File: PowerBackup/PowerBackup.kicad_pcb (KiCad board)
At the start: 4 copper layers, 40 x 41 mm, 70 parts, among them J1 Conn_01x02_Female, J10 Conn_01x02_Female, J2 Conn_01x07_Male, J3 Conn_01x04_Male, J4 Conn_01x05_Female, J5 Conn_01x04_Male, J6 Conn_01x02_Female, J7 Conn_01x02_Male, J8 Conn_01x02_Female, J9 Conn_01x02_Female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

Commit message: Added BOM and production files
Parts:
- added R24: 100, Resistor_SMD:R_0805_2012Metric, B.Cu at (131.0, 105.6)
- R12, R9: footprint Resistor_SMD:R_0805_2012Metric -> Resistor_SMD:R_0603_1608Metric
- R14: value 200 -> 100
- R18: value 1.5k -> 1k
- TH1: value Thermistor_NTC -> 10k
- moved R14 2.85 mm to (128.2, 106.3), turned to -90 degrees
- moved C18 0.23 mm to (126.5, 98.8)
- moved R21 0.22 mm to (123.7, 100.1)
- moved J9 0.18 mm to (124.1, 115.3)
- moved C16 0.17 mm to (129.2, 98.4)
- moved C17 0.17 mm to (130.7, 98.4)
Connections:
- net Net-(J3-Pad3) renamed /PrimaryBatteryMonitoring/SDA
- net Net-(J3-Pad4) renamed /PrimaryBatteryMonitoring/SCL
- C1 pad 2: GNDS -> GND
- C11 pad 2: GNDS -> GND
- C2 pad 2: GNDS -> GND
- C25 pad 2: GNDS -> GND
- C3 pad 2: GNDS -> GND
- C4 pad 2: GNDS -> GND
- C5 pad 2: GNDS -> GND
- C6 pad 2: GNDS -> GND
- C7 pad 2: GNDS -> GND
- C8 pad 2: GNDS -> GND
- C9 pad 2: GNDS -> GND
- J3 pad 1: GNDS -> GND
- J5 pad 1: GNDS -> GND
- R10 pad 2: GNDS -> GND
- R12 pad 2: GNDS -> GND
- R23 pad 2: GNDS -> GND
- TH1 pad 2: GNDS -> GND
- U1 pad 10: GNDS -> GND
- U1 pad 16: Net-(R14-Pad1) -> Net-(R24-Pad1)
- U2 pad 23: GNDS -> GND
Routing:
- net GND: track 14.0 -> 17.8 mm, vias 29 -> 88
- net GNDS: track 3.78 -> 0.00 mm, vias 32 -> 0
- net Net-(R24-Pad1): track 0.00 -> 2.90 mm
- net Net-(J4-Pad2): track 7.33 -> 8.47 mm
- net Net-(R14-Pad1): track 2.90 -> 2.19 mm
- added copper zone on In2.Cu, net GND
- removed copper zone on B.Cu, net GNDS
- removed copper zone on F.Cu, net GNDS
- removed copper zone on In2.Cu, net GNDS
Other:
- board text added: "+5V"
- board text added: "+9V"
- board text added: "GND"
- board text added: "SCL"
- board text added: "SDA"
- board text added: "VBAT+"

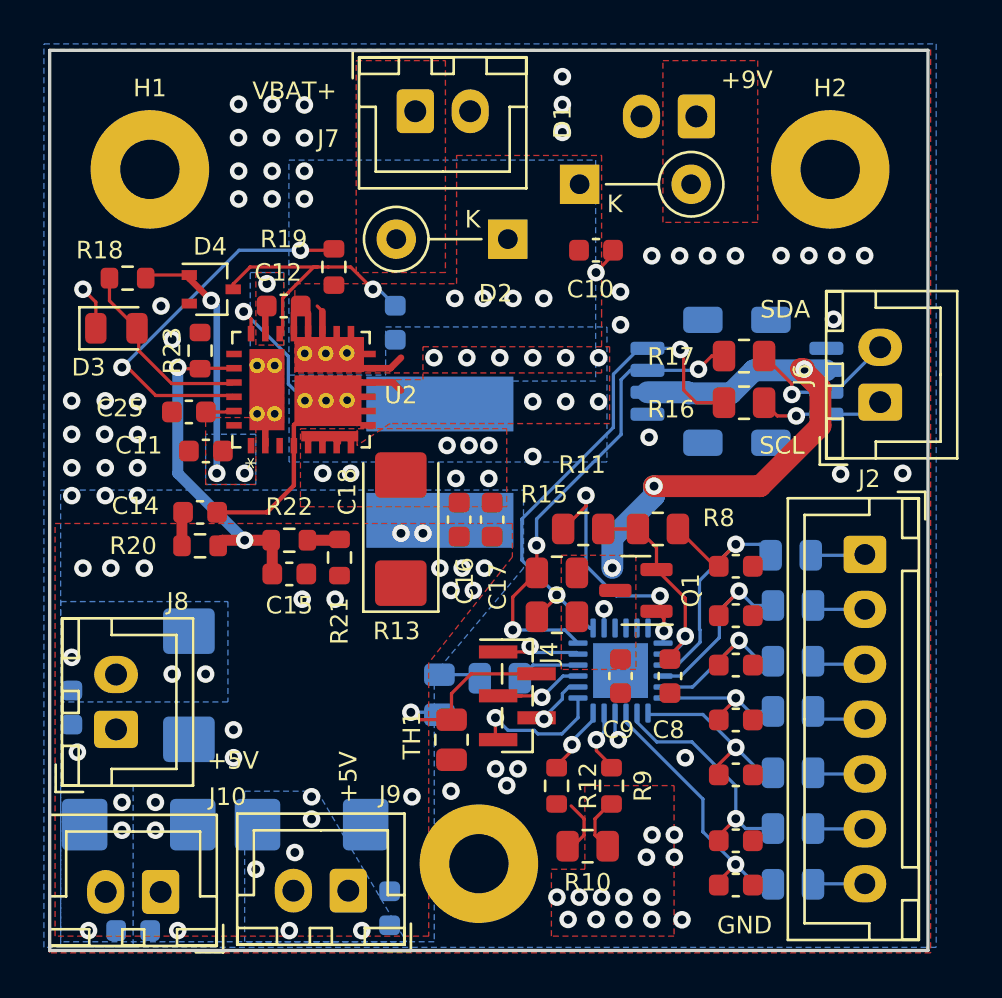
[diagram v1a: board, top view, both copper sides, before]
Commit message: Pvin is connected to Vin through a 2.21R resistor
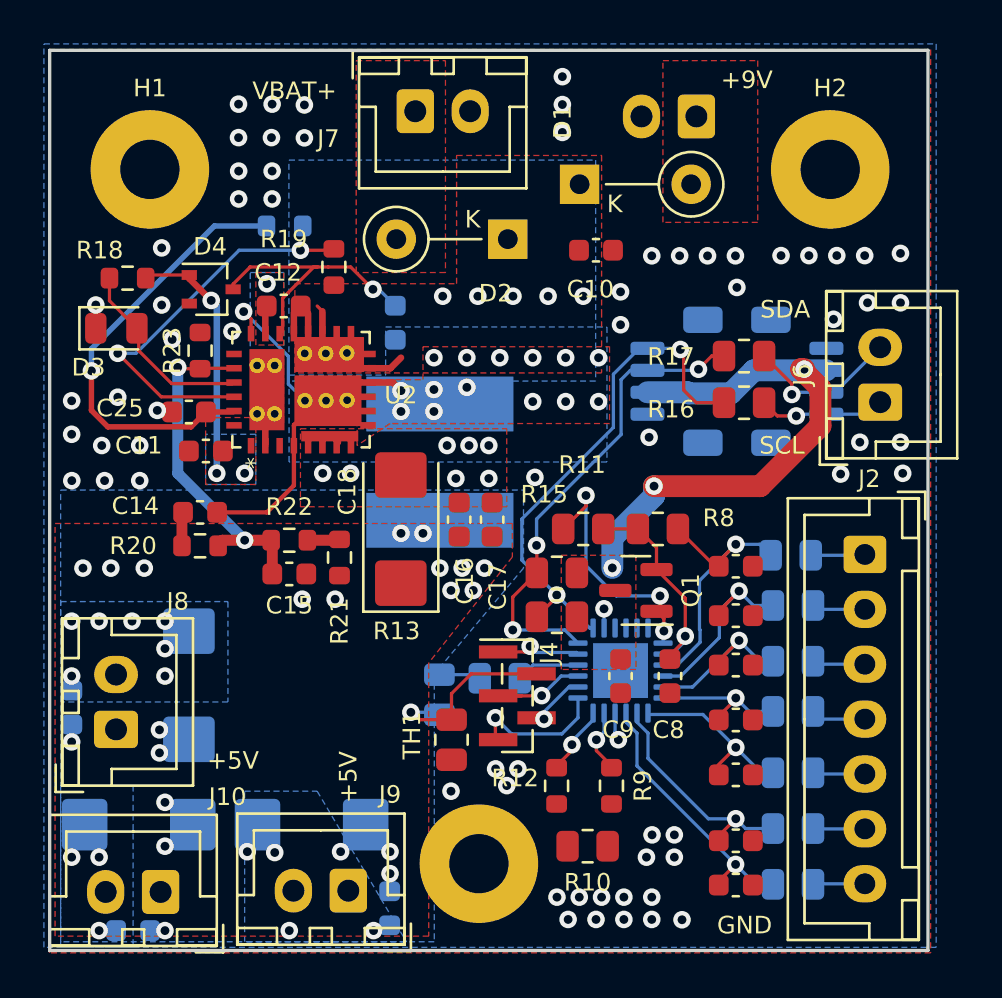
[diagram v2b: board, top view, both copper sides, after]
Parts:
- added R25: 2.21R, Resistor_SMD:R_0603_1608Metric, B.Cu at (121.2, 85.0)
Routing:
- net Net-(C25-Pad1): track 1.63 -> 20.2 mm, vias 0 -> 1
- net GND: track 17.8 -> 10.7 mm, vias 88 -> 89
- net /Backup/SW: vias 10 -> 15
- net +9VA: vias 0 -> 5
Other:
- board text added: "This is gonna work"
